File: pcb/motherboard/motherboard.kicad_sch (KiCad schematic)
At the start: 0 parts

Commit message: added MCU component to motherboard design
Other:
- added sheet STM32 (stm32.kicad_sch)
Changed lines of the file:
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@@
 	(generator_version "10.0")
 	(paper "A4")
+	(sheet
+		(at 60.96 44.45)
+		(size 16.51 21.59)
+		(exclude_from_sim no)
+		(in_bom yes)
+		(on_board yes)
+		(dnp no)
+		(fields_autoplaced yes)
+		(stroke
+			(width 0.1524)
+			(type solid)
+		)
+		(fill
+			(color 0 0 0 0)
+		)
+		(property "Sheetname" "STM32"
+			(at 60.96 43.7384 0)
+			(show_name no)
+			(do_not_autoplace no)
+			(effects
+				(font
+					(size 1.27 1.27)
+				)
+				(justify left bottom)
+			)
+		)
+		(property "Sheetfile" "stm32.kicad_sch"
+			(at 60.96 66.6246 0)
+			(show_name no)
+			(do_not_autoplace no)
+			(effects
+				(font
+					(size 1.27 1.27)
+				)
+				(justify left top)
+			)
+		)
+		(instances
+			(project "motherboard"
+				(path "/dd0de6d4-7020-4d4a-9487-5c8f4729c64b"
+					(page "2")
+				)
+			)
+		)
+	)
 	(sheet_instances
 		(path "/"

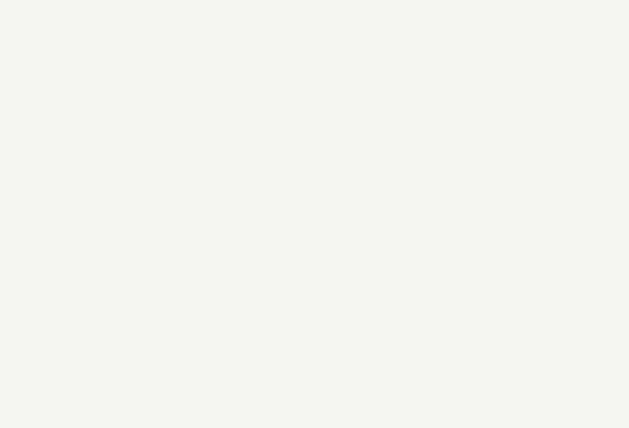
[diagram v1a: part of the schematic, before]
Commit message: DaughterBoard Selector Schematic Finished SPI decoder using 74HC138
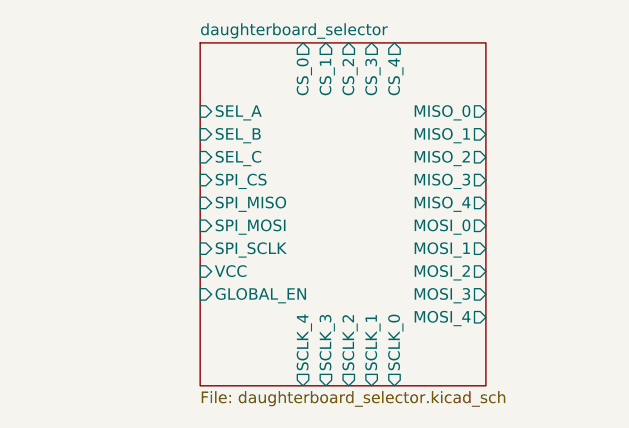
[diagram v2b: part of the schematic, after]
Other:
- added sheet daughterboard_selector (daughterboard_selector.kicad_sch)

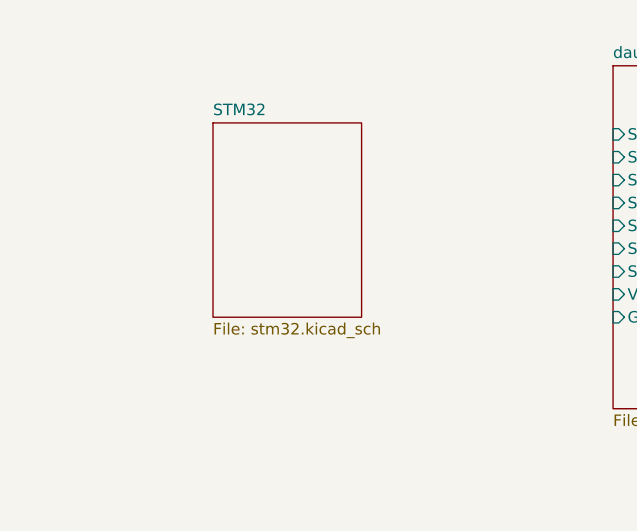
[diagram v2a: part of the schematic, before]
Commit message: added MCU hierarchy labels
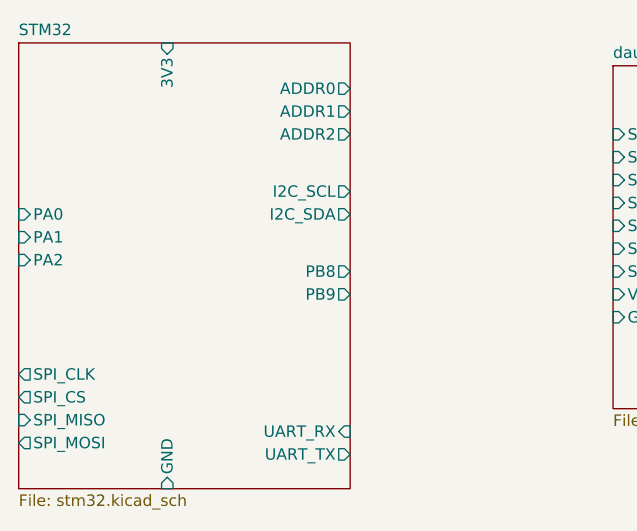
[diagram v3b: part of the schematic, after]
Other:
- sheet STM32 ports: added 3V3, ADDR0, ADDR1, ADDR2, GND, I2C_SCL, I2C_SDA, PA0, PA1, PA2, PB8, PB9, SPI_CLK, SPI_CS, SPI_MISO, SPI_MOSI, UART_RX, UART_TX; removed none
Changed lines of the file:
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@@
 	(paper "A4")
 	(sheet
-		(at 60.96 44.45)
-		(size 16.51 21.59)
+		(at 39.37 35.56)
+		(size 36.83 49.53)
 		(exclude_from_sim no)
 		(in_bom yes)
@@
 		)
 		(property "Sheetname" "STM32"
-			(at 60.96 43.7384 0)
+			(at 39.37 34.8484 0)
 			(show_name no)
 			(do_not_autoplace no)
@@
 		)
 		(property "Sheetfile" "stm32.kicad_sch"
-			(at 60.96 66.6246 0)
+			(at 39.37 85.6746 0)
 			(show_name no)
 			(do_not_autoplace no)
@@
 			)
 		)
+		(pin "3V3" input
+			(at 55.88 35.56 90)
+			(effects
+				(font
+					(size 1.27 1.27)
+				)
+				(justify right)
+			)
+		)
+		(pin "ADDR0" output
+			(at 76.2 40.64 0)
+			(effects
+				(font
+					(size 1.27 1.27)
+				)
+				(justify right)
+			)
+		)
+		(pin "ADDR1" output
+			(at 76.2 43.18 0)
+			(effects
+				(font
+					(size 1.27 1.27)
+				)
+				(justify right)
+			)
+		)
+		(pin "ADDR2" output
+			(at 76.2 45.72 0)
+			(effects
+				(font
+					(size 1.27 1.27)
+				)
+				(justify right)
+			)
+		)
+		(pin "GND" input
+			(at 55.88 85.09 270)
+			(effects
+				(font
+					(size 1.27 1.27)
+				)
+				(justify left)
+			)
+		)
+		(pin "I2C_SCL" output
+			(at 76.2 52.07 0)
+			(effects
+				(font
+					(size 1.27 1.27)
+				)
+				(justify right)
+			)
+		)
+		(pin "I2C_SDA" output
+			(at 76.2 54.61 0)
+			(effects
+				(font
+					(size 1.27 1.27)
+				)
+				(justify right)
+			)
+		)
+		(pin "PA0" input
+			(at 39.37 54.61 180)
+			(effects
+				(font
+					(size 1.27 1.27)
+				)
+				(justify left)
+			)
+		)
+		(pin "PA1" input
+			(at 39.37 57.15 180)
+			(effects
+				(font
+					(size 1.27 1.27)
+				)
+				(justify left)
+			)
+		)
+		(pin "PA2" input
+			(at 39.37 59.69 180)
+			(effects
+				(font
+					(size 1.27 1.27)
+				)
+				(justify left)
+			)
+		)
+		(pin "PB8" output
+			(at 76.2 60.96 0)
+			(effects
+				(font
+					(size 1.27 1.27)
+				)
+				(justify right)
+			)
+		)
+		(pin "PB9" output
+			(at 76.2 63.5 0)
+			(effects
+				(font
+					(size 1.27 1.27)
+				)
+				(justify right)
+			)
+		)
+		(pin "SPI_CLK" output
+			(at 39.37 72.39 180)
+			(effects
+				(font
+					(size 1.27 1.27)
+				)
+				(justify left)
+			)
+		)
+		(pin "SPI_CS" output
+			(at 39.37 74.93 180)
+			(effects
+				(font
+					(size 1.27 1.27)
+				)
+				(justify left)
+			)
+		)
+		(pin "SPI_MISO" input
+			(at 39.37 77.47 180)
+			(effects
+				(font
+					(size 1.27 1.27)
+				)
+				(justify left)
+			)
+		)
+		(pin "SPI_MOSI" output
+			(at 39.37 80.01 180)
+			(effects
+				(font
+					(size 1.27 1.27)
+				)
+				(justify left)
+			)
+		)
+		(pin "UART_RX" input
+			(at 76.2 78.74 0)
+			(effects
+				(font
+					(size 1.27 1.27)
+				)
+				(justify right)
+			)
+		)
+		(pin "UART_TX" output
+			(at 76.2 81.28 0)
+			(effects
+				(font
+					(size 1.27 1.27)
+				)
+				(justify right)
+			)
+		)

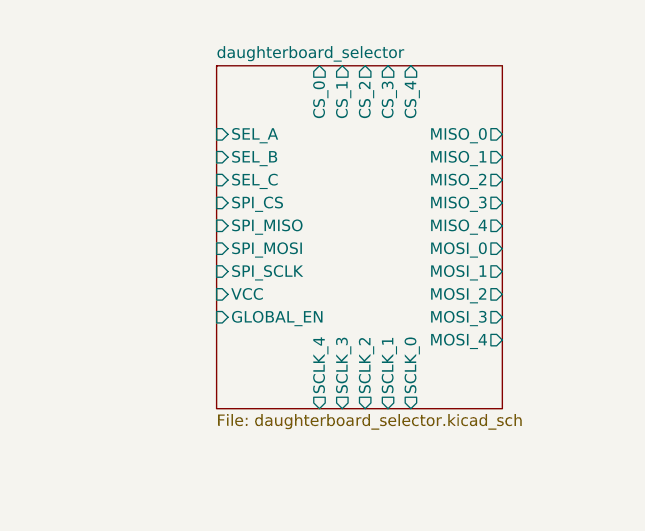
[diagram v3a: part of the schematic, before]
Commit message: Fix DaughterBoard Selector use 74HC138 exclusively for Chip Select.
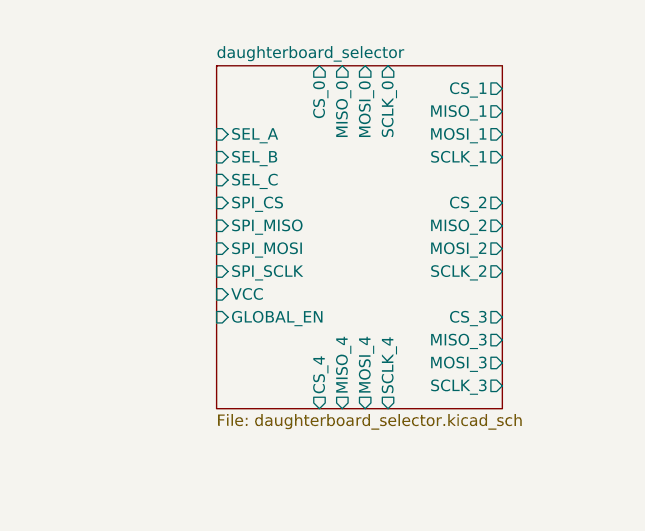
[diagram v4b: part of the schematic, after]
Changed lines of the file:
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@@
 		)
 		(pin "CS_1" output
-			(at 119.38 38.1 90)
+			(at 137.16 40.64 0)
 			(effects
 				(font
@@
 		)
 		(pin "CS_2" output
-			(at 121.92 38.1 90)
+			(at 137.16 53.34 0)
 			(effects
 				(font
@@
 		)
 		(pin "CS_3" output
-			(at 124.46 38.1 90)
+			(at 137.16 66.04 0)
 			(effects
 				(font
@@
 		)
 		(pin "CS_4" output
-			(at 127 38.1 90)
+			(at 116.84 76.2 270)
 			(effects
 				(font
 					(size 1.27 1.27)
 				)
-				(justify right)
+				(justify left)
 			)
 		)
@@
 		)
 		(pin "MISO_0" output
+			(at 119.38 38.1 90)
+			(effects
+				(font
+					(size 1.27 1.27)
+				)
+				(justify right)
+			)
+		)
+		(pin "MISO_1" output
+			(at 137.16 43.18 0)
+			(effects
+				(font
+					(size 1.27 1.27)
+				)
+				(justify right)
+			)
+		)
+		(pin "MISO_2" output
+			(at 137.16 55.88 0)
+			(effects
+				(font
+					(size 1.27 1.27)
+				)
+				(justify right)
+			)
+		)
+		(pin "MISO_3" output
+			(at 137.16 68.58 0)
+			(effects
+				(font
+					(size 1.27 1.27)
+				)
+				(justify right)
+			)
+		)
+		(pin "MISO_4" output
+			(at 119.38 76.2 270)
+			(effects
+				(font
+					(size 1.27 1.27)
+				)
+				(justify left)
+			)
+		)
+		(pin "MOSI_0" output
+			(at 121.92 38.1 90)
+			(effects
+				(font
+					(size 1.27 1.27)
+				)
+				(justify right)
+			)
+		)
+		(pin "MOSI_1" output
 			(at 137.16 45.72 0)
 			(effects
@@
 			)
 		)
-		(pin "MISO_1" output
+		(pin "MOSI_2" output
+			(at 137.16 58.42 0)
+			(effects
+				(font
+					(size 1.27 1.27)
+				)
+				(justify right)
+			)
+		)
+		(pin "MOSI_3" output
+			(at 137.16 71.12 0)
+			(effects
+				(font
+					(size 1.27 1.27)
+				)
+				(justify right)
+			)
+		)
+		(pin "MOSI_4" output
+			(at 121.92 76.2 270)
+			(effects
+				(font
+					(size 1.27 1.27)
+				)
+				(justify left)
+			)
+		)
+		(pin "SCLK_0" output
+			(at 124.46 38.1 90)
+			(effects
+				(font
+					(size 1.27 1.27)
+				)
+				(justify right)
+			)
+		)
+		(pin "SCLK_1" output
 			(at 137.16 48.26 0)
 			(effects
@@
 			)
 		)
-		(pin "MISO_2" output
-			(at 137.16 50.8 0)
-			(effects
-				(font
-					(size 1.27 1.27)
-				)
-				(justify right)
-			)
-		)
-		(pin "MISO_3" output
-			(at 137.16 53.34 0)
-			(effects
-				(font
-					(size 1.27 1.27)
-				)
-				(justify right)
-			)
-		)
-		(pin "MISO_4" output
-			(at 137.16 55.88 0)
-			(effects
-				(font
-					(size 1.27 1.27)
-				)
-				(justify right)
-			)
-		)
-		(pin "MOSI_0" output
-			(at 137.16 58.42 0)
-			(effects
-				(font
-					(size 1.27 1.27)
-				)
-				(justify right)
-			)
-		)
-		(pin "MOSI_1" output
+		(pin "SCLK_2" output
 			(at 137.16 60.96 0)
 			(effects
@@
 			)
 		)
-		(pin "MOSI_2" output
-			(at 137.16 63.5 0)
+		(pin "SCLK_3" output
+			(at 137.16 73.66 0)
 			(effects
 				(font
@@
 			)
 		)
-		(pin "MOSI_3" output
-			(at 137.16 66.04 0)
-			(effects
-				(font
-					(size 1.27 1.27)
-				)
-				(justify right)
-			)
-		)
-		(pin "MOSI_4" output
-			(at 137.16 68.58 0)
-			(effects
-				(font
-					(size 1.27 1.27)
-				)
-				(justify right)
-			)
-		)
-		(pin "SCLK_0" output
-			(at 127 76.2 270)
-			(effects
-				(font
-					(size 1.27 1.27)
-				)
-				(justify left)
-			)
-		)
-		(pin "SCLK_1" output
+		(pin "SCLK_4" output
 			(at 124.46 76.2 270)
 			(effects
 				(font
-					(size 1.27 1.27)
-				)
-				(justify left)
-			)
-		)
-		(pin "SCLK_2" output
-			(at 121.92 76.2 270)
-			(effects
-				(font
-					(size 1.27 1.27)
-				)
-				(justify left)
-			)
-		)
-		(pin "SCLK_3" output
-			(at 119.38 76.2 270)
-			(effects
-				(font
-					(size 1.27 1.27)
-				)
-				(justify left)
-			)
-		)
-		(pin "SCLK_4" output
-			(at 116.84 76.2 270)
-			(effects
-				(font

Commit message: motherboard design update
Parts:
- added C12, C13, C14: 100nF, symbol Device:C_Small
- added C15: 100nF, Capacitor_SMD:C_0603_1608Metric, symbol Device:C_Small
- added J3: UART_USB, Connector_USB:USB_C_Receptacle_Amphenol_12401948E412A, symbol Connector:USB_C_Receptacle_USB2.0_16P
- added J4: I2C_HEADER, symbol Connector:Conn_01x04_Pin
- added R4, R5, R6: 10k, symbol Device:R_Small_US
- added R7, R8: 5.1k, symbol Device:R_Small_US
- added SW2: GEN_MAZE, symbol Switch:SW_Push
- added SW3: TOGGLE_MAZE, symbol Switch:SW_Push
- added SW4: SOLVE_MAZE, symbol Switch:SW_Push
- added U2: CH340C, Package_SO:SOIC-16_3.9x9.9mm_P1.27mm, symbol Interface_USB:CH340C
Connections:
- net STM32/I2C_SCL: now also J4.2 (Pin_2)
- net STM32/I2C_SDA: now also J4.3 (Pin_3)
- new net: J3.A4 (VBUS), J3.A9 (VBUS), J3.B4 (VBUS), J3.B9 (VBUS)
- new net: J3.A5 (CC1), R8.1
- new net: J3.B5 (CC2), R7.1
- new net +3V3: C15.1, R4.1, R5.1, R6.1, U2.16 (VCC), U2.4 (V3)
- new net +5V: J4.1 (Pin_1)
- new net GEN_MAZE: C12.2, R4.2, SW2.2
- new net GND: C12.1, C13.1, C14.1, C15.2, J3.A1 (GND), J3.A12 (GND), J3.B1 (GND), J3.B12 (GND), J3.SH (SHIELD), J4.4 (Pin_4), R7.2, R8.2, SW2.1, SW3.1, SW4.1, U2.1 (GND)
- new net SOLVE_MAZE: C14.2, R6.2, SW4.2
- new net TG_MAZE: C13.2, R5.2, SW3.2
- new net UART_RX: U2.2 (TXD)
- new net UART_TX: U2.3 (RXD)
- new net USB_D+: J3.A6 (D+), J3.B6 (D+), U2.5 (UD+)
- new net USB_D-: J3.A7 (D-), J3.B7 (D-), U2.6 (UD-)
- no-connect marks 0 -> 9
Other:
- added sheet power (power.kicad_sch)
